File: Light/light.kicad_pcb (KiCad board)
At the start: 2 copper layers, 4.6 x 15.7 mm, 5 parts, among them U1 4pin_light_conn

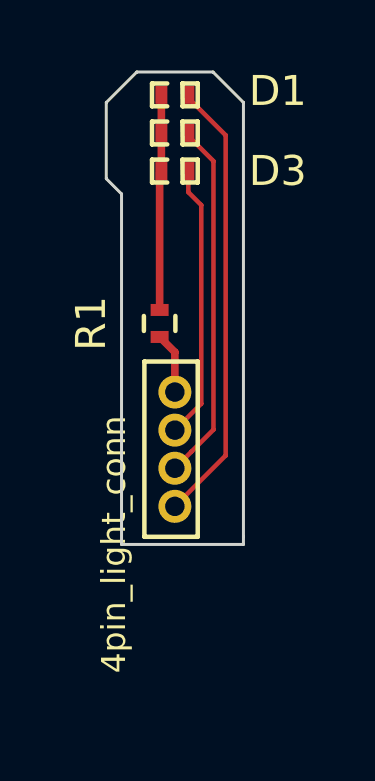
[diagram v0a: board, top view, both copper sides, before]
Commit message: removed an unnecessary resistor and redid the layout
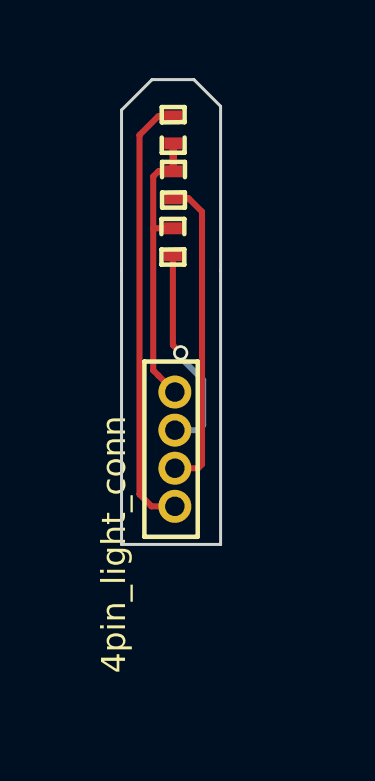
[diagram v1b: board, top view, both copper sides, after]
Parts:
- removed R1: R, Resistors_SMD:R_0402
- moved D3 2.36 mm to (163.3, 80.1), turned to 270 degrees
- moved D2 1.73 mm to (163.3, 78.2), turned to 270 degrees
- moved D1 1.17 mm to (163.3, 76.4), turned to 90 degrees
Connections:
- D1 pad 1: Net-(D1-Pad1) -> VIN
- D2 pad 1: Net-(D1-Pad1) -> VIN
- D3 pad 1: Net-(D1-Pad1) -> VIN
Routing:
- net VIN: track 2.05 -> 9.83 mm
- net Net-(D1-Pad1): track 7.19 -> 0.00 mm
- net PIN3: track 9.18 -> 7.10 mm, vias 0 -> 1
- net PIN2: track 12.1 -> 10.6 mm
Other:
- board size 4.6 x 15.7 mm -> 3.3 x 15.5 mm
